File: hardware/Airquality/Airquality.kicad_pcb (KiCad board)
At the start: 2 copper layers, 6 parts, among them J1 Conn_01x04_Female, J2 Conn_01x04_Female, U1 WeMos_D1_mini, U2 DS18B20, U3 PMS7003

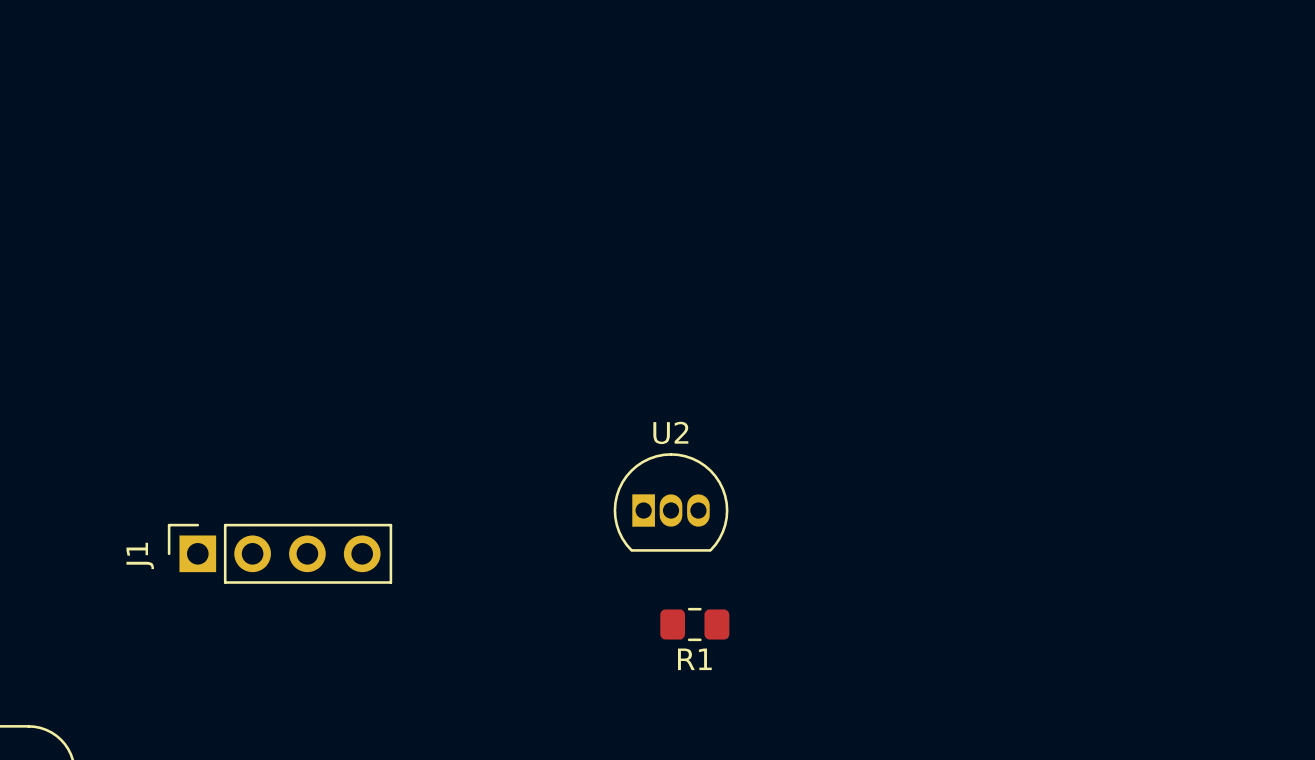
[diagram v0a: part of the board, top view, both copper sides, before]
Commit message: added 4 pinheaders for aliexpress i2c sensor modules
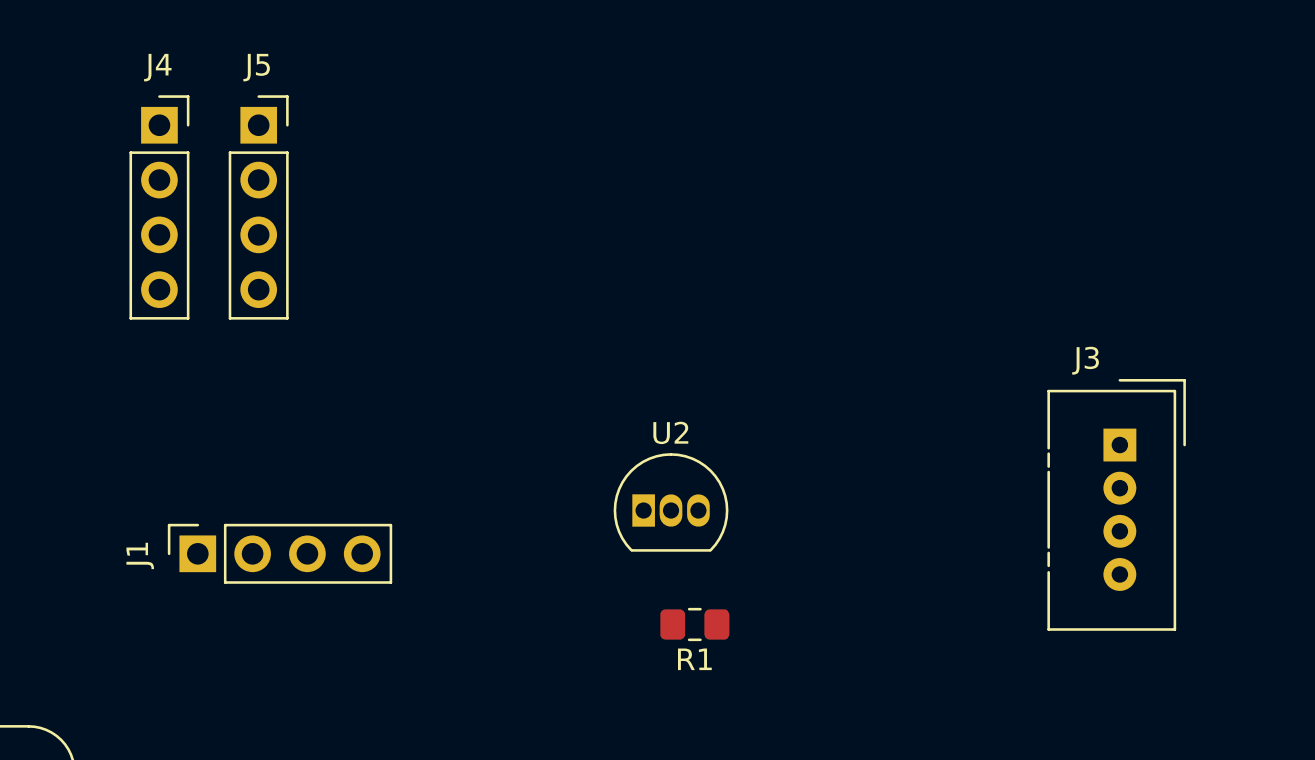
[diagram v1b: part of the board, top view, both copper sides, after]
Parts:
- added J3: Conn_01x04_Male, Connector:NS-Tech_Grove_1x04_P2mm_Vertical, F.Cu at (211.2, 76.6)
- added J4: Conn_01x04_Female, Connector_PinSocket_2.54mm:PinSocket_1x04_P2.54mm_Vertical, F.Cu at (166.7, 61.8)
- added J5: Conn_01x04_Female, Connector_PinSocket_2.54mm:PinSocket_1x04_P2.54mm_Vertical, F.Cu at (171.3, 61.8)
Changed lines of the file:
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@@
     (tracks 0)
     (zones 0)
-    (modules 6)
+    (modules 9)
     (nets 24)
   )
@@
     (add_net SDA)
   )
+  (module Connector_PinSocket_2.54mm:PinSocket_1x04_P2.54mm_Vertical (layer F.Cu)
+    (at 171.3129 61.7982)
+    (descr "Through hole straight socket strip, 1x04, 2.54mm pitch, single row (from Kicad 4.0.7), script generated")
+    (tags "Through hole socket strip THT 1x04 2.54mm single row")
+    (fp_text reference J5 (at 0 -2.77) (layer F.SilkS)
+      (effects (font (size 1 1) (thickness 0.15)))
+    )
+    (fp_text value Conn_01x04_Female (at 0 10.39) (layer F.Fab)
+      (effects (font (size 1 1) (thickness 0.15)))
+    )
+    (fp_text user %R (at 0 3.81 90) (layer F.Fab)
+      (effects (font (size 1 1) (thickness 0.15)))
+    )
+    (fp_line (start -1.27 -1.27) (end 0.635 -1.27) (layer F.Fab) (width 0.1))
+    (fp_line (start 0.635 -1.27) (end 1.27 -0.635) (layer F.Fab) (width 0.1))
+    (fp_line (start 1.27 -0.635) (end 1.27 8.89) (layer F.Fab) (width 0.1))
+    (fp_line (start 1.27 8.89) (end -1.27 8.89) (layer F.Fab) (width 0.1))
+    (fp_line (start -1.27 8.89) (end -1.27 -1.27) (layer F.Fab) (width 0.1))
+    (fp_line (start -1.33 1.27) (end 1.33 1.27) (layer F.SilkS) (width 0.12))
+    (fp_line (start -1.33 1.27) (end -1.33 8.95) (layer F.SilkS) (width 0.12))
+    (fp_line (start -1.33 8.95) (end 1.33 8.95) (layer F.SilkS) (width 0.12))
+    (fp_line (start 1.33 1.27) (end 1.33 8.95) (layer F.SilkS) (width 0.12))
+    (fp_line (start 1.33 -1.33) (end 1.33 0) (layer F.SilkS) (width 0.12))
+    (fp_line (start 0 -1.33) (end 1.33 -1.33) (layer F.SilkS) (width 0.12))
+    (fp_line (start -1.8 -1.8) (end 1.75 -1.8) (layer F.CrtYd) (width 0.05))
+    (fp_line (start 1.75 -1.8) (end 1.75 9.4) (layer F.CrtYd) (width 0.05))
+    (fp_line (start 1.75 9.4) (end -1.8 9.4) (layer F.CrtYd) (width 0.05))
+    (fp_line (start -1.8 9.4) (end -1.8 -1.8) (layer F.CrtYd) (width 0.05))
+    (pad 4 thru_hole oval (at 0 7.62) (size 1.7 1.7) (drill 1) (layers *.Cu *.Mask)
+      (net 1 SDA))
+    (pad 3 thru_hole oval (at 0 5.08) (size 1.7 1.7) (drill 1) (layers *.Cu *.Mask)
+      (net 2 SCL))
+    (pad 2 thru_hole oval (at 0 2.54) (size 1.7 1.7) (drill 1) (layers *.Cu *.Mask)
+      (net 3 GND))
+    (pad 1 thru_hole rect (at 0 0) (size 1.7 1.7) (drill 1) (layers *.Cu *.Mask)
+      (net 4 +3V3))
+    (model ${KISYS3DMOD}/Connector_PinSocket_2.54mm.3dshapes/PinSocket_1x04_P2.54mm_Vertical.wrl
+      (at (xyz 0 0 0))
+      (scale (xyz 1 1 1))
+      (rotate (xyz 0 0 0))
+    )
+  )
+  (module Connector_PinSocket_2.54mm:PinSocket_1x04_P2.54mm_Vertical (layer F.Cu)
+    (at 166.7129 61.7982)
+    (descr "Through hole straight socket strip, 1x04, 2.54mm pitch, single row (from Kicad 4.0.7), script generated")
+    (tags "Through hole socket strip THT 1x04 2.54mm single row")
+    (fp_text reference J4 (at 0 -2.77) (layer F.SilkS)
+      (effects (font (size 1 1) (thickness 0.15)))
+    )
+    (fp_text value Conn_01x04_Female (at 0 10.39) (layer F.Fab)
+      (effects (font (size 1 1) (thickness 0.15)))
+    )
+    (fp_text user %R (at 0 3.81 90) (layer F.Fab)
+      (effects (font (size 1 1) (thickness 0.15)))
+    )
+    (fp_line (start -1.27 -1.27) (end 0.635 -1.27) (layer F.Fab) (width 0.1))
+    (fp_line (start 0.635 -1.27) (end 1.27 -0.635) (layer F.Fab) (width 0.1))
+    (fp_line (start 1.27 -0.635) (end 1.27 8.89) (layer F.Fab) (width 0.1))
+    (fp_line (start 1.27 8.89) (end -1.27 8.89) (layer F.Fab) (width 0.1))
+    (fp_line (start -1.27 8.89) (end -1.27 -1.27) (layer F.Fab) (width 0.1))
+    (fp_line (start -1.33 1.27) (end 1.33 1.27) (layer F.SilkS) (width 0.12))
+    (fp_line (start -1.33 1.27) (end -1.33 8.95) (layer F.SilkS) (width 0.12))
+    (fp_line (start -1.33 8.95) (end 1.33 8.95) (layer F.SilkS) (width 0.12))
+    (fp_line (start 1.33 1.27) (end 1.33 8.95) (layer F.SilkS) (width 0.12))
+    (fp_line (start 1.33 -1.33) (end 1.33 0) (layer F.SilkS) (width 0.12))
+    (fp_line (start 0 -1.33) (end 1.33 -1.33) (layer F.SilkS) (width 0.12))
+    (fp_line (start -1.8 -1.8) (end 1.75 -1.8) (layer F.CrtYd) (width 0.05))
+    (fp_line (start 1.75 -1.8) (end 1.75 9.4) (layer F.CrtYd) (width 0.05))
+    (fp_line (start 1.75 9.4) (end -1.8 9.4) (layer F.CrtYd) (width 0.05))
+    (fp_line (start -1.8 9.4) (end -1.8 -1.8) (layer F.CrtYd) (width 0.05))
+    (pad 4 thru_hole oval (at 0 7.62) (size 1.7 1.7) (drill 1) (layers *.Cu *.Mask)
+      (net 1 SDA))
+    (pad 3 thru_hole oval (at 0 5.08) (size 1.7 1.7) (drill 1) (layers *.Cu *.Mask)
+      (net 2 SCL))
+    (pad 2 thru_hole oval (at 0 2.54) (size 1.7 1.7) (drill 1) (layers *.Cu *.Mask)
+      (net 3 GND))
+    (pad 1 thru_hole rect (at 0 0) (size 1.7 1.7) (drill 1) (layers *.Cu *.Mask)
+      (net 4 +3V3))
+    (model ${KISYS3DMOD}/Connector_PinSocket_2.54mm.3dshapes/PinSocket_1x04_P2.54mm_Vertical.wrl
+      (at (xyz 0 0 0))
+      (scale (xyz 1 1 1))
+      (rotate (xyz 0 0 0))
+    )
+  )
+  (module Connector:NS-Tech_Grove_1x04_P2mm_Vertical (layer F.Cu)
+    (at 211.2264 76.6191)
+    (descr https://statics3.seeedstudio.com/images/opl/datasheet/3470130P1.pdf)
+    (tags Grove-1x04)
+    (fp_text reference J3 (at -1.5 -4) (layer F.SilkS)
+      (effects (font (size 1 1) (thickness 0.15)))
+    )
+    (fp_text value Conn_01x04_Male (at 4.19 2.83 90) (layer F.Fab)
+      (effects (font (size 1 1) (thickness 0.15)))
+    )
+    (fp_text user %R (at -2 2 90) (layer F.Fab)
+      (effects (font (size 1 1) (thickness 0.15)))
+    )
+    (fp_line (start 0.9 0) (end 2.2 1) (layer F.Fab) (width 0.1))
+    (fp_line (start 2.2 -1) (end 0.9 0) (layer F.Fab) (width 0.1))
+    (fp_line (start 3 -3) (end 3 0) (layer F.SilkS) (width 0.12))
+    (fp_line (start 0 -3) (end 3 -3) (layer F.SilkS) (width 0.12))
+    (fp_line (start -3.45 -2.65) (end -3.45 8.7) (layer F.CrtYd) (width 0.05))
+    (fp_line (start -3.45 8.7) (end 2.7 8.7) (layer F.CrtYd) (width 0.05))
+    (fp_line (start 2.7 8.7) (end 2.7 -2.65) (layer F.CrtYd) (width 0.05))
+    (fp_line (start -3.45 -2.65) (end 2.7 -2.65) (layer F.CrtYd) (width 0.05))
+    (fp_line (start -3.3 5) (end -3.3 5.6) (layer F.SilkS) (width 0.12))
+    (fp_line (start -3.3 0.4) (end -3.3 1) (layer F.SilkS) (width 0.12))
+    (fp_line (start 2.55 -2.5) (end 2.55 8.55) (layer F.SilkS) (width 0.12))
+    (fp_line (start -3.3 -2.5) (end 2.55 -2.5) (layer F.SilkS) (width 0.12))
+    (fp_line (start -3.3 1.25) (end -3.3 4.75) (layer F.SilkS) (width 0.12))
+    (fp_line (start -3.3 8.55) (end 2.55 8.55) (layer F.SilkS) (width 0.12))
+    (fp_line (start -3.3 -2.5) (end -3.3 0.15) (layer F.SilkS) (width 0.12))
+    (fp_line (start -3.3 5.9) (end -3.3 8.55) (layer F.SilkS) (width 0.12))
+    (fp_line (start -2.9 -2.1) (end 2.2 -2.1) (layer F.Fab) (width 0.1))
+    (fp_line (start 2.2 -2.1) (end 2.2 8.1) (layer F.Fab) (width 0.1))
+    (fp_line (start 2.2 8.1) (end -2.9 8.1) (layer F.Fab) (width 0.1))
+    (fp_line (start -2.9 8.1) (end -2.9 -2.1) (layer F.Fab) (width 0.1))
+    (pad 4 thru_hole circle (at 0 6) (size 1.524 1.524) (drill 0.762) (layers *.Cu *.Mask)
+      (net 3 GND))
+    (pad 3 thru_hole circle (at 0 4) (size 1.524 1.524) (drill 0.762) (layers *.Cu *.Mask)
+      (net 4 +3V3))
+    (pad 2 thru_hole circle (at 0 2) (size 1.524 1.524) (drill 0.762) (layers *.Cu *.Mask)
+      (net 1 SDA))
+    (pad 1 thru_hole rect (at 0 0) (size 1.524 1.524) (drill 0.762) (layers *.Cu *.Mask)
+      (net 2 SCL))
+    (model ${KISYS3DMOD}/Connector.3dshapes/NS-Tech_Grove_1x04_P2mm_Vertical.wrl
+      (at (xyz 0 0 0))
+      (scale (xyz 0.3937 0.3937 0.3937))
+      (rotate (xyz 0 0 -90))
+    )
+  )
   (module PMS7003:PMS7003 (layer F.Cu)
